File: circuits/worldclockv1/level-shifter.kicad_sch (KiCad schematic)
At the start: 18 parts, among them Q1 BSS138, Q2 BSS138, Q3 BSS138, Q4 BSS138, Q5 BSS138, Q6 BSS138

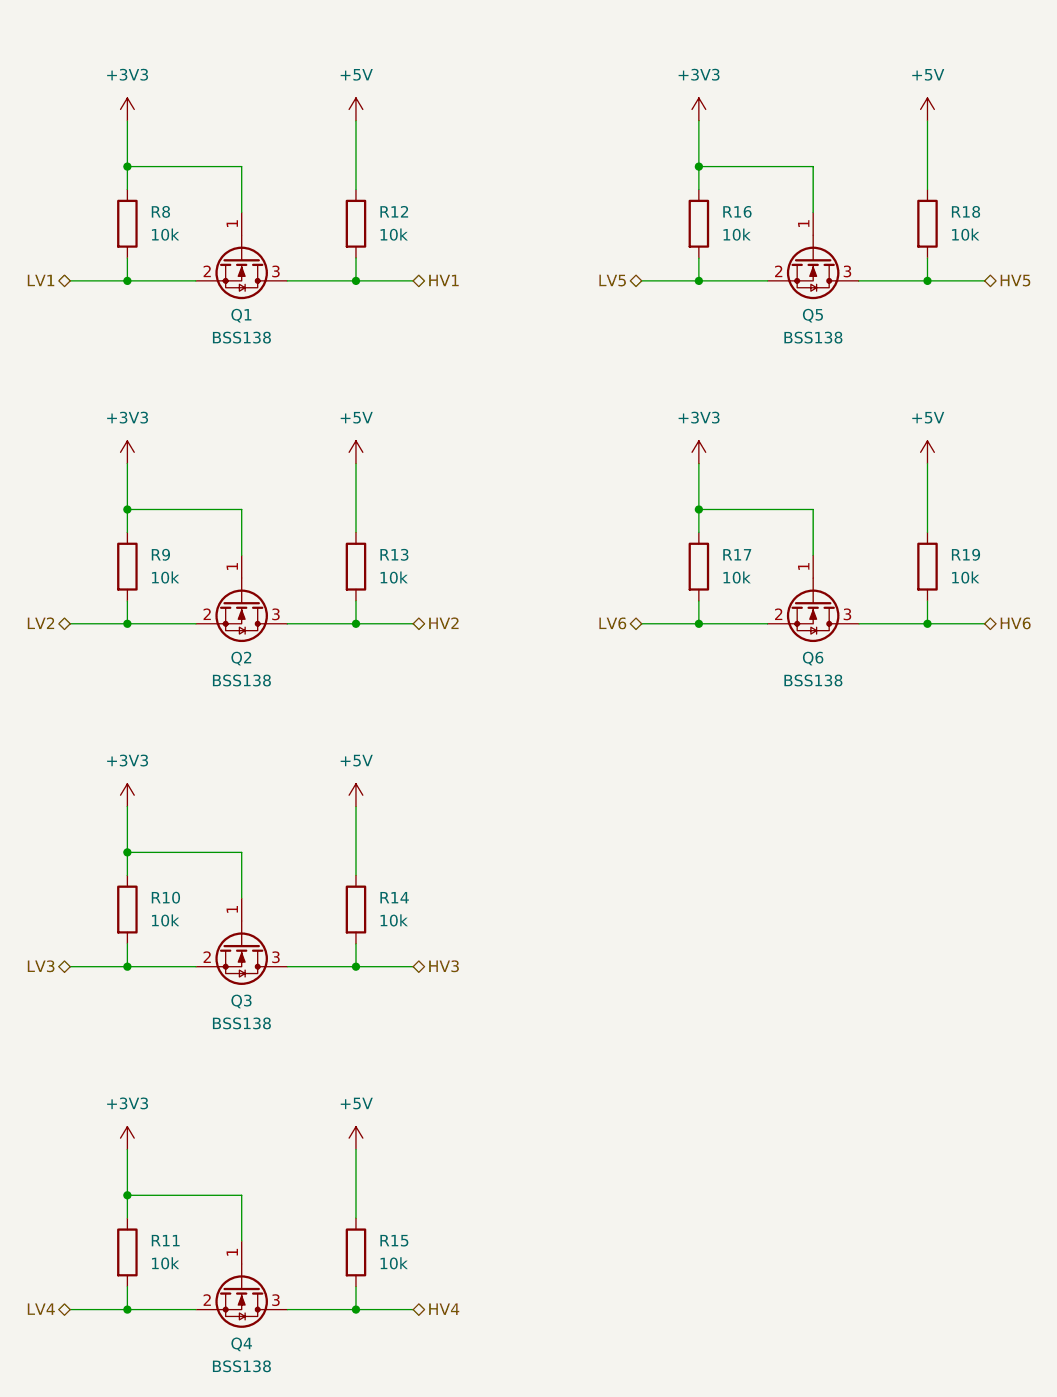
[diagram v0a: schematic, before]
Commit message: World Clock PCB completed
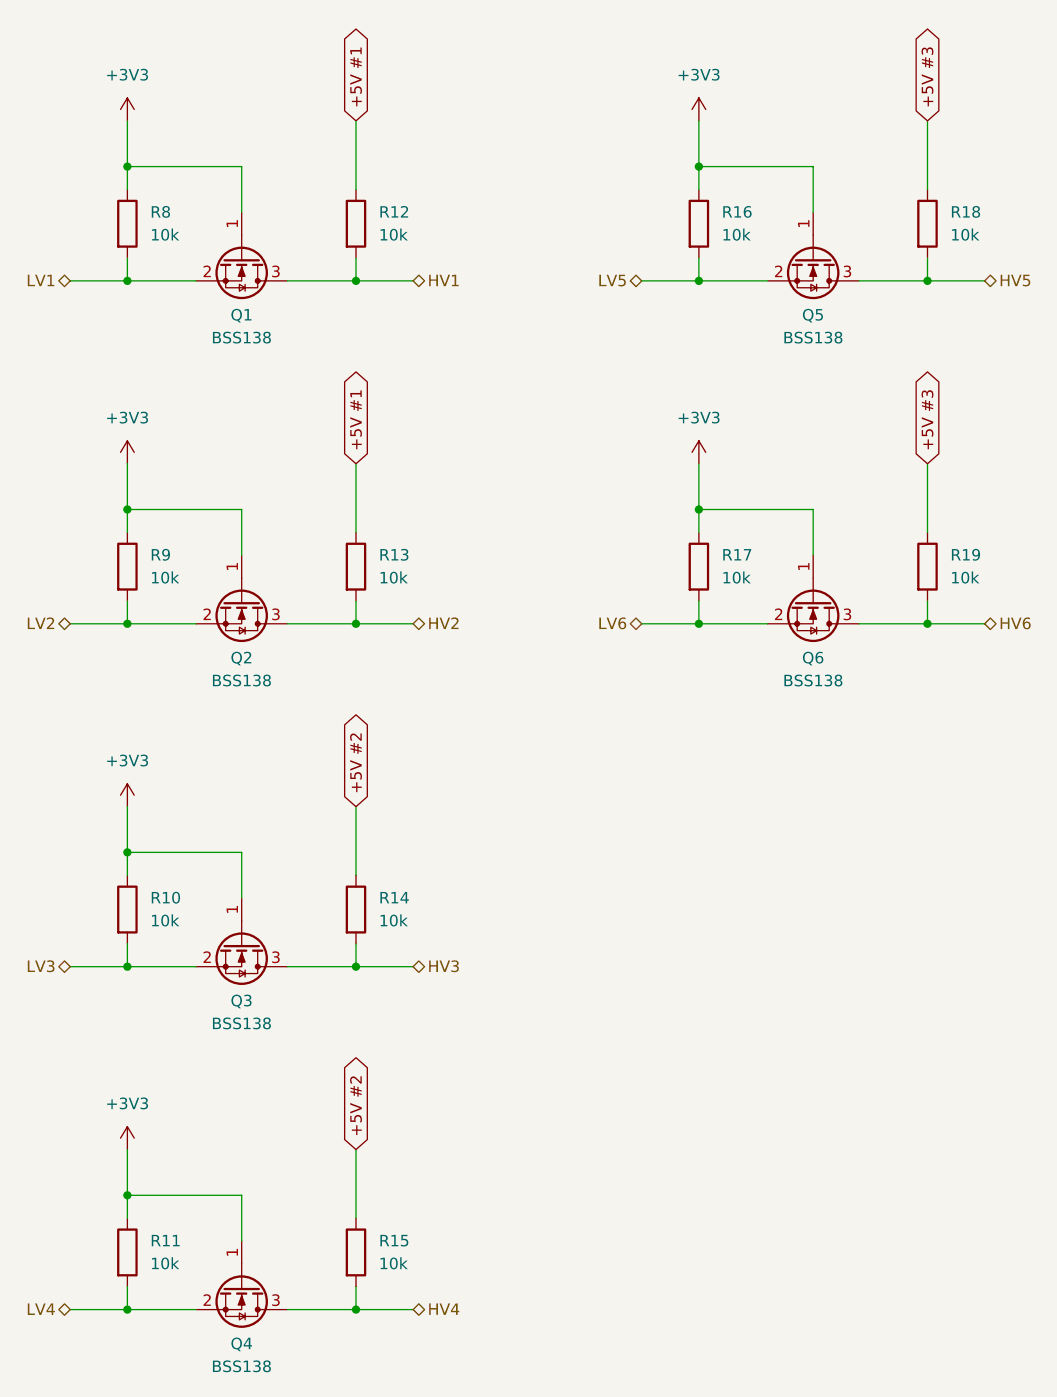
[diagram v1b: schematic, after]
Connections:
- removed net +5V: R12.1, R13.1, R14.1, R15.1, R18.1, R19.1
- new net +5V #1: R12.1, R13.1
- new net +5V #2: R14.1, R15.1
- new net +5V #3: R18.1, R19.1
